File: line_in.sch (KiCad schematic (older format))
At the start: 4 parts, among them J9 JACK_TRS_5PINS

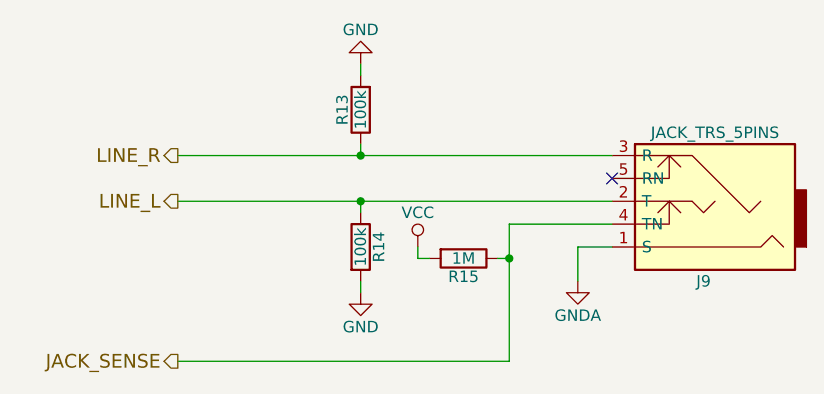
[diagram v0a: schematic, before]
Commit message: Major update to use Atmel ATTINY4313
Replace Pro Micro as microcontroller. Mostly contianed within the
control sheet.
Moved LEDs all onto control sheet.
Updated a few capacitors.
Added a reset switch. Still need to decide part.
Updated a few capacitor models for 4.0.7
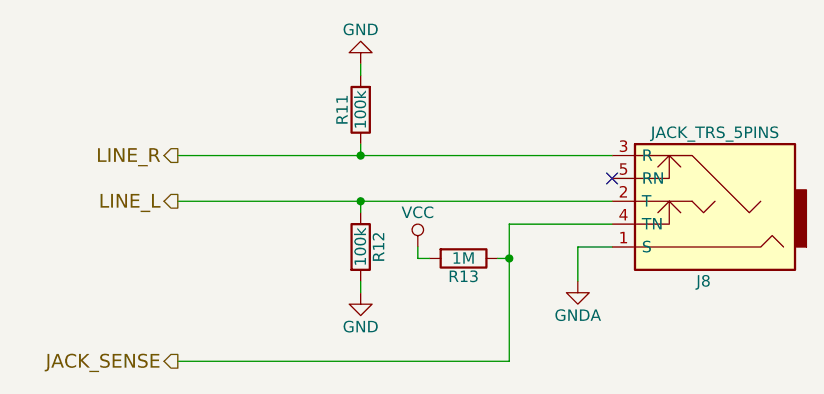
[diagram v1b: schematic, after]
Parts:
- renumbered J9 to J8, R13 to R11, R14 to R12, R15 to R13
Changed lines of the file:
@@
 $Descr USLetter 11000 8500
 encoding utf-8
-Sheet 9 10
+Sheet 8 10
 Title ""
 Date ""
@@
 $EndDescr
 $Comp
-L JACK_TRS_5PINS J9
+L JACK_TRS_5PINS J8
 U 1 1 595D415D
 P 6700 3350
-F 0 "J9" H 6700 3700 50  0000 C CNN
+F 0 "J8" H 6700 3700 50  0000 C CNN
 F 1 "JACK_TRS_5PINS" H 6650 3050 50  0000 C CNN
 F 2 "blubaru:sj1-353xng" H 6800 3200 50  0001 C CNN
-F 3 "http://www.cui.com/product/resource/sj1-352xng-series.pdf" H 6800 3200 50  0001 C CNN
+F 3 "http://www.cui.com/product/resource/sj1-353xng.pdf" H 6800 3200 50  0001 C CNN
 	1    6700 3350
 	-1   0    0    1
@@
 	4400 3350 6300 3350
 $Comp
-L R R13
+L R R11
 U 1 1 595F0365
 P 5200 2950
-F 0 "R13" V 5280 2950 50  0000 C CNN
+F 0 "R11" V 5280 2950 50  0000 C CNN
 F 1 "100k" V 5200 2950 50  0000 C CNN
 F 2 "Resistors_THT:R_Axial_DIN0204_L3.6mm_D1.6mm_P5.08mm_Horizontal" V 5130 2950 50  0001 C CNN
@@
 $EndComp
 $Comp
-L GND #PWR035
+L GND #PWR030
 U 1 1 595F03CA
 P 5200 2750
-F 0 "#PWR035" H 5200 2500 50  0001 C CNN
+F 0 "#PWR030" H 5200 2500 50  0001 C CNN
 F 1 "GND" H 5200 2600 50  0000 C CNN
 F 2 "" H 5200 2750 50  0001 C CNN
@@
 Connection ~ 5850 3600
 $Comp
-L GND #PWR036
+L GND #PWR031
 U 1 1 595F0532
 P 5200 3750
-F 0 "#PWR036" H 5200 3500 50  0001 C CNN
+F 0 "#PWR031" H 5200 3500 50  0001 C CNN
 F 1 "GND" H 5200 3600 50  0000 C CNN
 F 2 "" H 5200 3750 50  0001 C CNN
@@
 $EndComp
 $Comp
-L R R14
+L R R12
 U 1 1 595F054E
 P 5200 3550
-F 0 "R14" V 5280 3550 50  0000 C CNN
+F 0 "R12" V 5280 3550 50  0000 C CNN
 F 1 "100k" V 5200 3550 50  0000 C CNN
 F 2 "Resistors_THT:R_Axial_DIN0204_L3.6mm_D1.6mm_P5.08mm_Horizontal" V 5130 3550 50  0001 C CNN
@@
 	5850 3450 5850 4050
 $Comp
-L R R15
+L R R13
 U 1 1 595F0435
 P 5650 3600
-F 0 "R15" V 5730 3600 50  0000 C CNN
+F 0 "R13" V 5730 3600 50  0000 C CNN
 F 1 "1M" V 5650 3600 50  0000 C CNN
 F 2 "Resistors_THT:R_Axial_DIN0204_L3.6mm_D1.6mm_P5.08mm_Horizontal" V 5580 3600 50  0001 C CNN
@@
 	5450 3600 5500 3600
 $Comp
-L VCC #PWR037
+L VCC #PWR032
 U 1 1 5971D586
 P 5450 3550
-F 0 "#PWR037" H 5450 3400 50  0001 C CNN
+F 0 "#PWR032" H 5450 3400 50  0001 C CNN
 F 1 "VCC" H 5450 3700 50  0000 C CNN
 F 2 "" H 5450 3550 50  0001 C CNN
@@
 $EndComp
 $Comp
-L GNDA #PWR038
+L GNDA #PWR033
 U 1 1 59C09A2F
 P 6150 3700
-F 0 "#PWR038" H 6150 3450 50  0001 C CNN
+F 0 "#PWR033" H 6150 3450 50  0001 C CNN
 F 1 "GNDA" H 6150 3550 50  0000 C CNN
 F 2 "" H 6150 3700 50  0000 C CNN

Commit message: Add LEDs to BT module
These already exist on the breakout board, but they will be more visible
if I add resistors to the front panel. They can be removed if space is
limited and the case is translucent, but add them for now. In V2, there
won't be a breakout board, so adding them now makes the V1 to V2 fewer
changes.
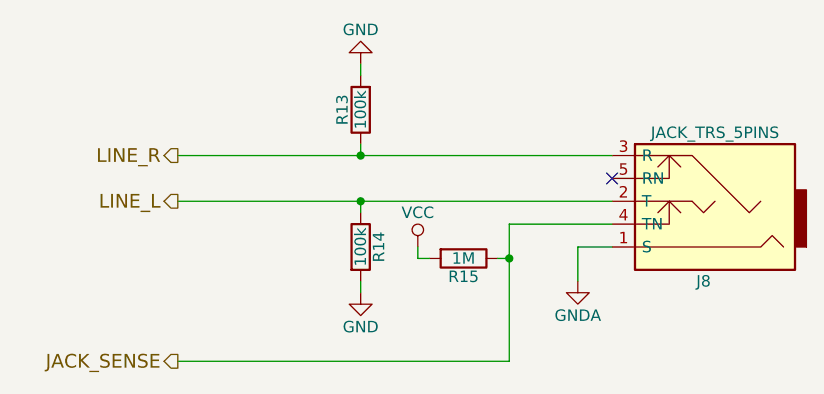
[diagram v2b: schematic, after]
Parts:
- renumbered R11 to R13, R12 to R14, R13 to R15
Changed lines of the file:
@@
 	4400 3350 6300 3350
 $Comp
-L R R11
+L R R13
 U 1 1 595F0365
 P 5200 2950
-F 0 "R11" V 5280 2950 50  0000 C CNN
+F 0 "R13" V 5280 2950 50  0000 C CNN
 F 1 "100k" V 5200 2950 50  0000 C CNN
 F 2 "Resistors_THT:R_Axial_DIN0204_L3.6mm_D1.6mm_P5.08mm_Horizontal" V 5130 2950 50  0001 C CNN
@@
 $EndComp
 $Comp
-L GND #PWR030
+L GND #PWR031
 U 1 1 595F03CA
 P 5200 2750
-F 0 "#PWR030" H 5200 2500 50  0001 C CNN
+F 0 "#PWR031" H 5200 2500 50  0001 C CNN
 F 1 "GND" H 5200 2600 50  0000 C CNN
 F 2 "" H 5200 2750 50  0001 C CNN
@@
 Connection ~ 5850 3600
 $Comp
-L GND #PWR031
+L GND #PWR032
 U 1 1 595F0532
 P 5200 3750
-F 0 "#PWR031" H 5200 3500 50  0001 C CNN
+F 0 "#PWR032" H 5200 3500 50  0001 C CNN
 F 1 "GND" H 5200 3600 50  0000 C CNN
 F 2 "" H 5200 3750 50  0001 C CNN
@@
 $EndComp
 $Comp
-L R R12
+L R R14
 U 1 1 595F054E
 P 5200 3550
-F 0 "R12" V 5280 3550 50  0000 C CNN
+F 0 "R14" V 5280 3550 50  0000 C CNN
 F 1 "100k" V 5200 3550 50  0000 C CNN
 F 2 "Resistors_THT:R_Axial_DIN0204_L3.6mm_D1.6mm_P5.08mm_Horizontal" V 5130 3550 50  0001 C CNN
@@
 	5850 3450 5850 4050
 $Comp
-L R R13
+L R R15
 U 1 1 595F0435
 P 5650 3600
-F 0 "R13" V 5730 3600 50  0000 C CNN
+F 0 "R15" V 5730 3600 50  0000 C CNN
 F 1 "1M" V 5650 3600 50  0000 C CNN
 F 2 "Resistors_THT:R_Axial_DIN0204_L3.6mm_D1.6mm_P5.08mm_Horizontal" V 5580 3600 50  0001 C CNN
@@
 	5450 3600 5500 3600
 $Comp
-L VCC #PWR032
+L VCC #PWR033
 U 1 1 5971D586
 P 5450 3550
-F 0 "#PWR032" H 5450 3400 50  0001 C CNN
+F 0 "#PWR033" H 5450 3400 50  0001 C CNN
 F 1 "VCC" H 5450 3700 50  0000 C CNN
 F 2 "" H 5450 3550 50  0001 C CNN
@@
 $EndComp
 $Comp
-L GNDA #PWR033
+L GNDA #PWR034
 U 1 1 59C09A2F
 P 6150 3700
-F 0 "#PWR033" H 6150 3450 50  0001 C CNN
+F 0 "#PWR034" H 6150 3450 50  0001 C CNN
 F 1 "GNDA" H 6150 3550 50  0000 C CNN
 F 2 "" H 6150 3700 50  0000 C CNN
